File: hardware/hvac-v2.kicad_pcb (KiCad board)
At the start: 2 copper layers, 125 x 93 mm, 143 parts, among them J1 Anderson_two_redblack, J10 Conn_01x02, J11 Conn_01x03, J12 Conn_01x03, J13 Conn_01x03, J14 Conn_01x04, J2 Conn_01x04, J3 Conn_01x02, J4 Anderson_two_redblack_src, J5 Conn_01x03, J6 Conn_01x03, J7 Anderson_two_redblack_sink, J8 Anderson_two_redblack_sink, J9 Conn_01x02, Q1 AO3400A, Q2 AO3400A, Q3 AO3400A, SW1 SW_Push, SW2 Rotary_Encoder_Switch, U1 STM32F030C8Tx, U2 IFX007T, U3 IFX007T, U4 AMS1117-3.3, U5 DS18B20, U6 AMS1117-5.0

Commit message: Start hardware revision 2.3: fix LCD I2C
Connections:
- U1 pad 35: unconnected-(U1-Pad35) -> /SCL
- U1 pad 36: unconnected-(U1-Pad36) -> /SDA
- U1 pad 5: /SDA -> unconnected-(U1-Pad5)
- U1 pad 6: /SCL -> unconnected-(U1-Pad6)
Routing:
- net GND: track 601.7 -> 617.8 mm, vias 97 -> 98
- net /SCL: track 48.1 -> 63.8 mm, vias 0 -> 2
- net /SDA: track 46.2 -> 60.9 mm, vias 0 -> 2
- net unconnected-(U1-Pad6): track 0.00 -> 0.91 mm
- net unconnected-(U1-Pad5): track 0.00 -> 0.77 mm
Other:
- board text added: "hvac-v2.3"
- board text removed: "hvac-v2.2"

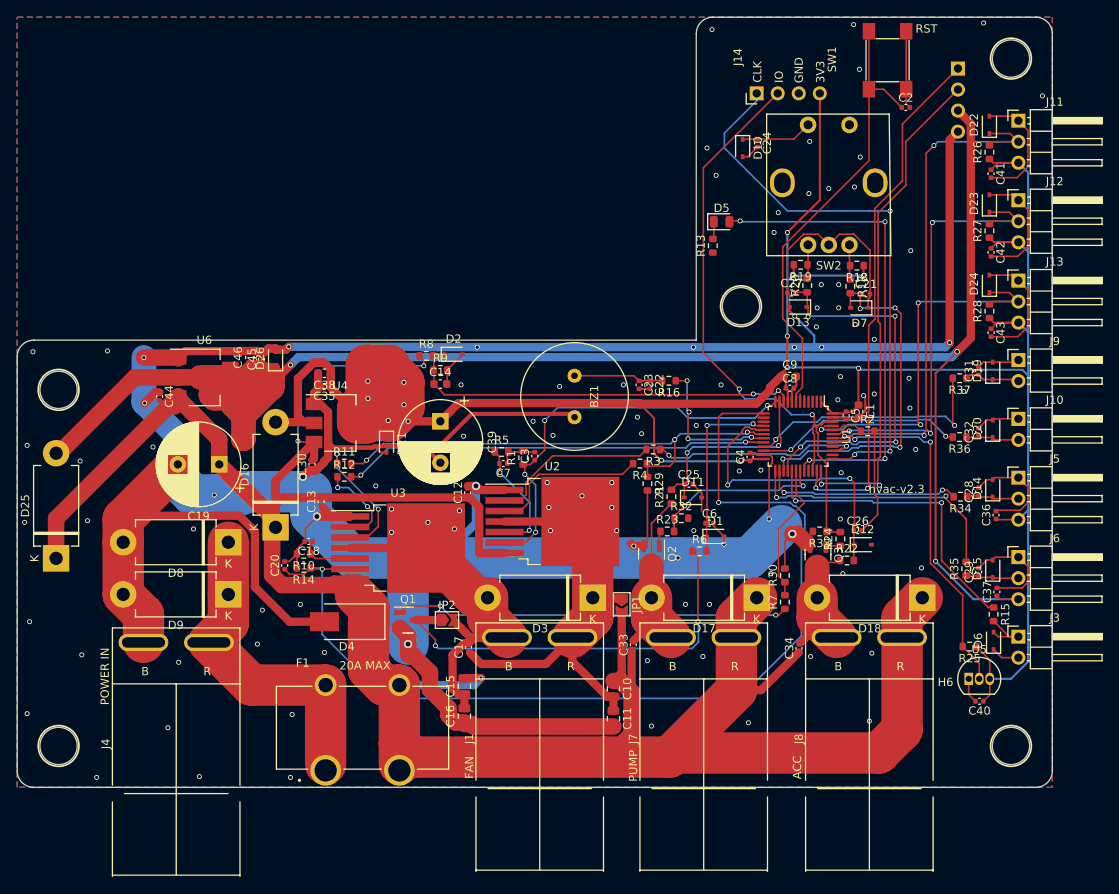
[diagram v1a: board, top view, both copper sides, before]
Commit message: Complete hardware v2.3:
- Fix LCD I2C pins
- Switch to voltage regulators with higher input voltage range
- Increase 12v line TVS diodes
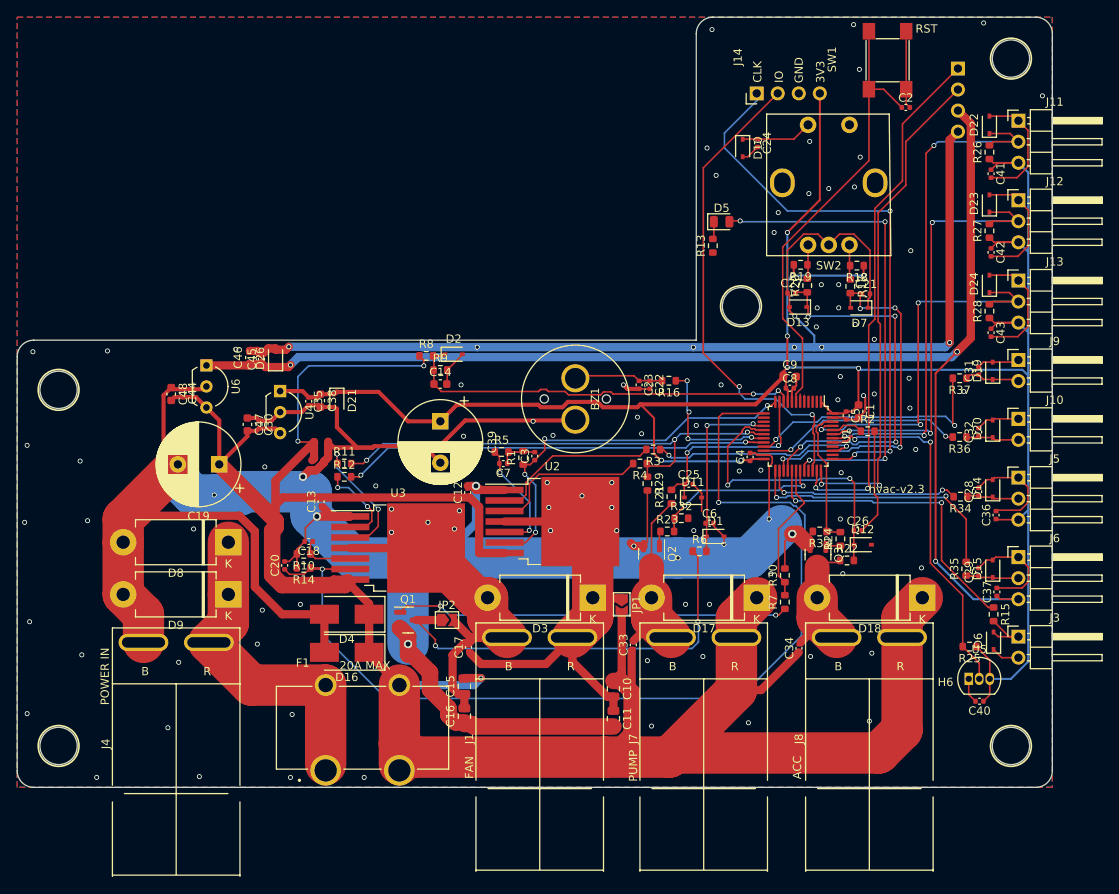
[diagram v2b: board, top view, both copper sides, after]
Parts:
- removed D25: D_Schottky, Diode_THT:D_DO-201AD_P12.70mm_Horizontal
- added C47: 4.7uF, Capacitor_SMD:C_0603_1608Metric, F.Cu at (57.8, 108.2)
- added C48: 4.7uF, Capacitor_SMD:C_0603_1608Metric, F.Cu at (48.6, 104.5)
- C39: value 1000uF -> 470uF
- D16: value D_Schottky -> TVS_12V; footprint Diode_THT:D_DO-201AD_P12.70mm_Horizontal -> Diode_SMD:D_SMB_Handsoldering
- U4: value AMS1117-3.3 -> AP7381-XXV; footprint Package_TO_SOT_SMD:SOT-223-3_TabPin2 -> Package_TO_SOT_THT:TO-92L_Inline_Wide
- U6: value AMS1117-5.0 -> AP7381-XXV; footprint Package_TO_SOT_SMD:SOT-223-3_TabPin2 -> Package_TO_SOT_THT:TO-92L_Inline_Wide
- moved D16 17.4 mm to (69.8, 135.7), turned to 180 degrees
- moved U4 8.21 mm to (61.8, 104.2), turned to -90 degrees
- moved C30 8.00 mm to (59.2, 108.2), turned to -90 degrees
- moved D21 7.94 mm to (68.6, 105.3)
- moved C38 3.34 mm to (66.6, 105.3), turned to -90 degrees
- moved C44 2.83 mm to (50.0, 104.4)
- moved C35 2.60 mm to (65.2, 105.4), turned to -90 degrees
- moved U6 1.47 mm to (52.9, 101.0), turned to -90 degrees
- moved D4 0.90 mm to (69.8, 131.1)
- moved BZ1 0.32 mm to (97.4, 105.1)
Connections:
- D16 pad 2: VCC -> GND
- U4 pad 1: GND -> VCC
- U4 pad 2: VCC -> GND
- U6 pad 1: GND -> +5V
- U6 pad 2: +5V -> GND
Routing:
- net +5V: track 213.3 -> 163.2 mm
- net VCC: track 326.4 -> 281.4 mm, vias 14 -> 8
- net +BATT: track 316.0 -> 302.2 mm
- net GND: track 617.8 -> 614.4 mm, vias 98 -> 96
- net /BRIDGE_SENSE_P: track 49.8 -> 47.6 mm

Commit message: Hardware revision 2.4:
- Actually wire encoder button to processor
- Increase power trace widths
- Fix encoder RC circuit cap size
- Add silk labels on top
- Add protection resistors to all IO
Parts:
- added Q4: AO3400A, Package_TO_SOT_SMD:SOT-23, F.Cu at (80.3, 135.5)
- added R31: 1k, Resistor_SMD:R_0603_1608Metric, F.Cu at (108.8, 107.2)
- added R38: 1k, Resistor_SMD:R_0603_1608Metric, F.Cu at (85.7, 104.5)
- added R39: 150, Resistor_SMD:R_0603_1608Metric, F.Cu at (122.7, 132.8)
- added R40: 1k, Resistor_SMD:R_0603_1608Metric, F.Cu at (116.7, 106.9)
- added R41: 1k, Resistor_SMD:R_0603_1608Metric, F.Cu at (116.8, 78.3)
- added R42: 150, Resistor_SMD:R_0603_1608Metric, F.Cu at (144.2, 132.2)
- added R43: 150, Resistor_SMD:R_0603_1608Metric, F.Cu at (139.8, 77.1)
- added R44: 150, Resistor_SMD:R_0603_1608Metric, F.Cu at (140.7, 85.9)
- added R45: 150, Resistor_SMD:R_0603_1608Metric, F.Cu at (138.8, 95.7)
- C10, C11, C15, C16: value 0.22uF -> 220nF
- C12, C13, C17, C18, C2, C22, C23, C24, C25, C26, C28, C29, C30, C31, C32, C33, C34, C35, C36, C37, C4, C40, C41, C42, C43, C44, C45, C5, C6, C7, C8: value 0.1uF -> 100nF
- C21, C27: value 0.1uF -> 10nF
- R34, R35, R36, R37: value 150 -> 1k
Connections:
- C14 pad 1: /VBATT_DIV -> Net-(C14-Pad1)
- C20 pad 1: /BRIDGE_SENSE_N -> Net-(C20-Pad1)
- C24 pad 1: /BUTTON -> Net-(C24-Pad1)
- C3 pad 1: /BRIDGE_SENSE_P -> Net-(C3-Pad1)
- D10 pad 1: /BUTTON -> Net-(C24-Pad1)
- D2 pad 1: /VBATT_DIV -> Net-(C14-Pad1)
- D22 pad 1: /TEMP_INSIDE -> Net-(D22-Pad1)
- D23 pad 1: /TEMP_OUTSIDE -> Net-(D23-Pad1)
- D24 pad 1: /TEMP_AUX -> Net-(D24-Pad1)
- J11 pad 2: /TEMP_INSIDE -> Net-(D22-Pad1)
- J12 pad 2: /TEMP_OUTSIDE -> Net-(D23-Pad1)
- J13 pad 2: /TEMP_AUX -> Net-(D24-Pad1)
- R1 pad 1: /BRIDGE_SENSE_P -> Net-(C3-Pad1)
- R14 pad 1: /BRIDGE_SENSE_N -> Net-(C20-Pad1)
- R25 pad 2: /TEMP_BUILTIN -> Net-(R25-Pad2)
- R26 pad 2: /TEMP_INSIDE -> Net-(D22-Pad1)
- R27 pad 2: /TEMP_OUTSIDE -> Net-(D23-Pad1)
- R28 pad 2: /TEMP_AUX -> Net-(D24-Pad1)
- R8 pad 2: /VBATT_DIV -> Net-(C14-Pad1)
- R9 pad 1: /VBATT_DIV -> Net-(C14-Pad1)
- SW2 pad S1: /BUTTON -> Net-(C24-Pad1)
- U1 pad 14: unconnected-(U1-Pad14) -> /BUTTON
- U2 pad 6: /BRIDGE_SENSE_P -> Net-(C3-Pad1)
- U3 pad 6: /BRIDGE_SENSE_N -> Net-(C20-Pad1)
- U5 pad 2: /TEMP_BUILTIN -> Net-(R25-Pad2)
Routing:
- net /BRIDGE_SENSE_N: track 123.9 -> 3.28 mm, vias 2 -> 0
- net Net-(C20-Pad1): track 0.00 -> 119.6 mm, vias 0 -> 2
- net Net-(Q4-Pad1): track 0.00 -> 46.3 mm, vias 0 -> 2
- net Net-(C3-Pad1): track 0.00 -> 33.9 mm, vias 0 -> 4
- net /BRIDGE_SENSE_P: track 47.6 -> 14.3 mm, vias 4 -> 2
- net /BUTTON: track 8.62 -> 38.3 mm, vias 0 -> 4
- net /TEMP_AUX: track 48.4 -> 25.6 mm, vias 3 -> 2
- net /TEMP_INSIDE: track 64.9 -> 43.0 mm, vias 3 -> 2
- net Net-(D24-Pad1): track 0.00 -> 21.1 mm, vias 0 -> 1
- net /TEMP_OUTSIDE: track 55.7 -> 35.0 mm, vias 3 -> 2
- net Net-(D22-Pad1): track 0.00 -> 20.2 mm, vias 0 -> 1
- net Net-(D23-Pad1): track 0.00 -> 19.6 mm, vias 0 -> 1
- net GND: track 614.4 -> 597.4 mm, vias 96 -> 95
- net Net-(C24-Pad1): track 0.00 -> 12.7 mm
- net /VBATT_DIV: track 49.4 -> 38.4 mm
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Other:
- board text added: "SW1"
- board text added: "SW2"
- board text added: "SW3"
- board text added: "TEMP_IN"
- board text added: "hvac-v2.4"
- board text removed: "hvac-v2.3"
